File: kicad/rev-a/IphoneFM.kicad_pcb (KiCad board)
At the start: 2 copper layers, 46.5 x 71.4 mm, 106 parts, among them J1 USB 2.0 Type-C, J2 SMA jack, SW1 SPDT, SW2 SPST, SW3 6 × SPST, U1 MCU, U2 Synthesizer, U3 3.3 V 600 mA LDO, U4 FM receiver, U5 SPDT RF switch, U6 USB ESD array, U7 Digital step attenuator, Y2 20 MHz CMOS XO

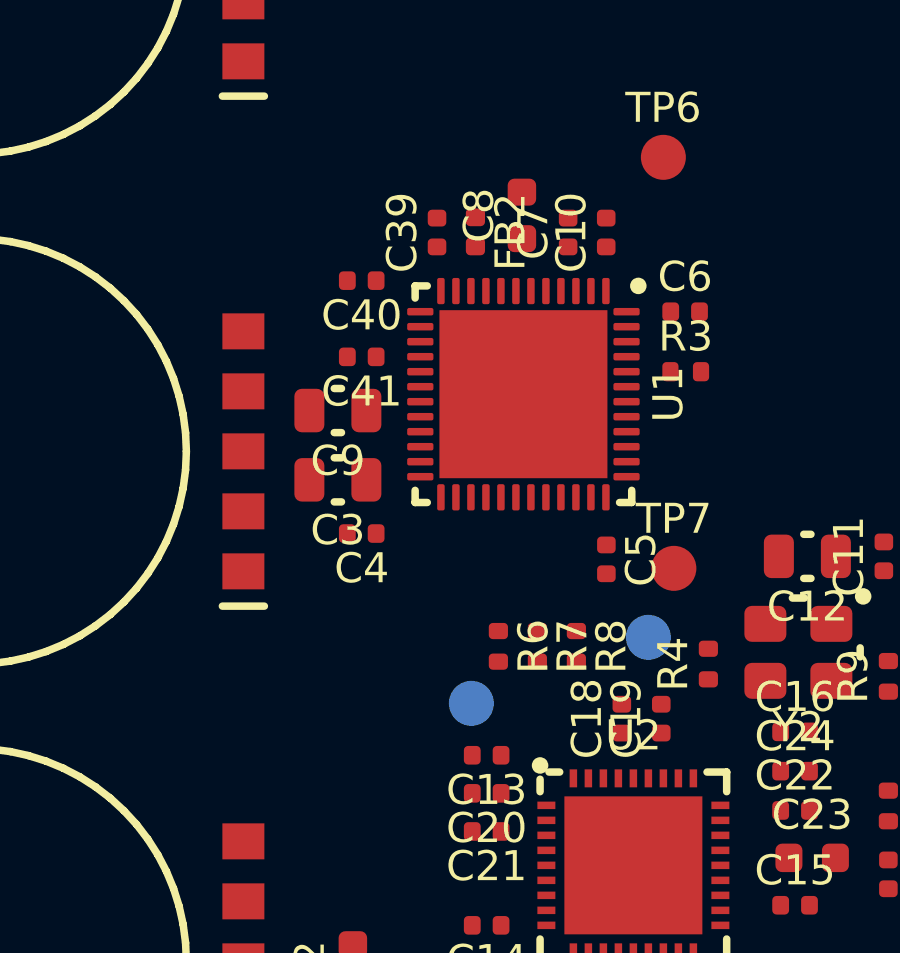
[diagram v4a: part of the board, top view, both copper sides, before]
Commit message: Phase 5 WIP: pcb_plan.py fan geometry, U1 escape plan (west and south, in progress), checker refinements; U1's west capacitors re-seated
Co-Authored-By: Claude Opus 5.5 <noreply@anthropic.com>
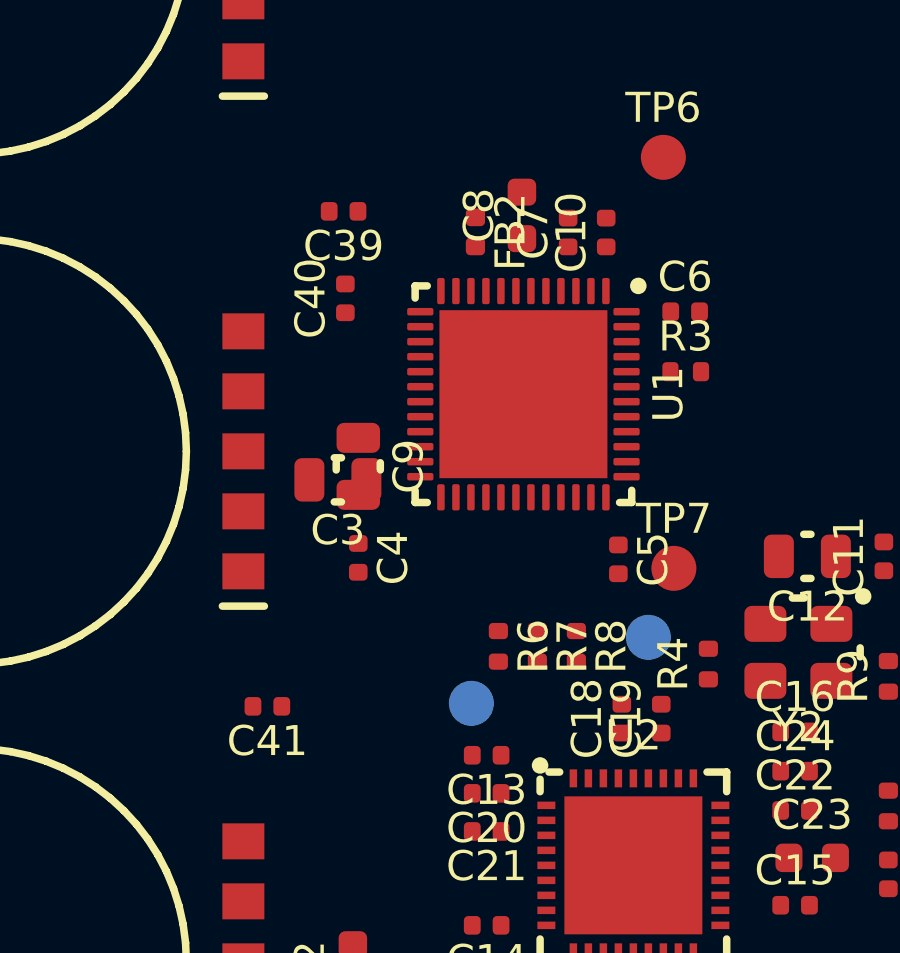
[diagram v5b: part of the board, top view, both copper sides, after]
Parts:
- moved C41 12.1 mm to (27.6, 103.5)
- moved C39 3.19 mm to (30.1, 87.0), turned to 180 degrees
- moved C9 1.98 mm to (30.6, 95.5), turned to -90 degrees
- moved C4 0.82 mm to (30.6, 98.5), turned to -90 degrees
- moved C40 0.80 mm to (30.2, 89.9), turned to 90 degrees
- moved C5 0.40 mm to (39.3, 98.6)
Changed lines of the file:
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@@
 	(footprint "IphoneFM:C_0402_1005Metric"
 		(layer "F.Cu")
-		(at 30.745 97.74 180)
+		(at 30.63 98.55 -90)
 		(descr "Capacitor SMD 0402 (1005 Metric), square (rectangular) end terminal, IPC-7351 nominal, (Body size source: IPC-SM-782 page 76, https://www.pcb-3d.com/wordpress/wp-content/uploads/ipc-sm-782a_amendment_1_and_2.pdf)")
 		(tags "capacitor")
 		(property "Reference" "C4"
-			(at 0 -1.16 540)
+			(at 0 -1.16 270)
 			(layer "F.SilkS")
 			(effects
@@
 		)
 		(property "Value" "100 nF X7R 16 V"
-			(at 0 1.16 540)
+			(at 0 1.16 270)
 			(layer "F.Fab")
 			(effects
@@
 		)
 		(property "Datasheet" "~"
-			(at 0 0 540)
+			(at 0 0 270)
 			(layer "F.Fab")
 			(hide yes)
@@
 		)
 		(property "Description" ""
-			(at 0 0 540)
+			(at 0 0 270)
 			(layer "F.Fab")
 			(hide yes)
@@
 		)
 		(property "KiLib_Generator" "SMD_2terminal_chip_molded"
-			(at 0 0 540)
+			(at 0 0 270)
 			(layer "F.SilkS")
 			(hide yes)
@@
 		)
 		(property "MPN" "CL05B104KO5NNNC"
-			(at 0 0 540)
+			(at 0 0 270)
 			(unlocked yes)
 			(layer "F.Fab")
@@
 		)
 		(property "LCSC" "C1525"
-			(at 0 0 540)
+			(at 0 0 270)
 			(unlocked yes)
 			(layer "F.Fab")
@@
 		)
 		(property "Manufacturer" "Samsung"
-			(at 0 0 540)
+			(at 0 0 270)
 			(unlocked yes)
 			(layer "F.Fab")
@@
 		)
 		(fp_text user "${REFERENCE}"
-			(at 0 0 540)
+			(at 0 0 630)
 			(layer "F.Fab")
 			(effects
@@
 		)
 		(pad "1" smd roundrect
-			(at -0.48 0 180)
+			(at -0.48 0 270)
 			(size 0.56 0.62)
 			(layers "F.Cu" "F.Mask" "F.Paste")
@@
 		)
 		(pad "2" smd roundrect
-			(at 0.48 0 180)
+			(at 0.48 0 270)
 			(size 0.56 0.62)
 			(layers "F.Cu" "F.Mask" "F.Paste")
@@
 	(footprint "IphoneFM:C_0402_1005Metric"
 		(layer "F.Cu")
-		(at 33.255 87.705 90)
+		(at 30.14 87 180)
 		(descr "Capacitor SMD 0402 (1005 Metric), square (rectangular) end terminal, IPC-7351 nominal, (Body size source: IPC-SM-782 page 76, https://www.pcb-3d.com/wordpress/wp-content/uploads/ipc-sm-782a_amendment_1_and_2.pdf)")
 		(tags "capacitor")
 		(property "Reference" "C39"
-			(at 0 -1.16 90)
+			(at 0 -1.16 180)
 			(layer "F.SilkS")
 			(effects
@@
 		)
 		(property "Value" "100 nF X7R 16 V"
-			(at 0 1.16 90)
+			(at 0 1.16 180)
 			(layer "F.Fab")
 			(effects
@@
 		)
 		(property "Datasheet" "~"
-			(at 0 0 90)
+			(at 0 0 180)
 			(layer "F.Fab")
 			(hide yes)
@@
 		)
 		(property "Description" ""
-			(at 0 0 90)
+			(at 0 0 180)
 			(layer "F.Fab")
 			(hide yes)
@@
 		)
 		(property "KiLib_Generator" "SMD_2terminal_chip_molded"
-			(at 0 0 90)
+			(at 0 0 180)
 			(layer "F.SilkS")
 			(hide yes)
@@
 		)
 		(property "MPN" "CL05B104KO5NNNC"
-			(at 0 0 90)
+			(at 0 0 180)
 			(unlocked yes)
 			(layer "F.Fab")
@@
 		)
 		(property "LCSC" "C1525"
-			(at 0 0 90)
+			(at 0 0 180)
 			(unlocked yes)
 			(layer "F.Fab")
@@
 		)
 		(property "Manufacturer" "Samsung"
-			(at 0 0 90)
+			(at 0 0 180)
 			(unlocked yes)
 			(layer "F.Fab")
@@
 		)
 		(fp_text user "${REFERENCE}"
-			(at 0 0 450)
+			(at 0 0 540)
 			(layer "F.Fab")
 			(effects
@@
 		)
 		(pad "1" smd roundrect
-			(at -0.48 0 90)
+			(at -0.48 0 180)
 			(size 0.56 0.62)
 			(layers "F.Cu" "F.Mask" "F.Paste")
@@
 		)
 		(pad "2" smd roundrect
-			(at 0.48 0 90)
+			(at 0.48 0 180)
 			(size 0.56 0.62)
 			(layers "F.Cu" "F.Mask" "F.Paste")
@@
 	(footprint "IphoneFM:C_0402_1005Metric"
 		(layer "F.Cu")
-		(at 38.9 98.6 -90)
+		(at 39.3 98.6 -90)
 		(descr "Capacitor SMD 0402 (1005 Metric), square (rectangular) end terminal, IPC-7351 nominal, (Body size source: IPC-SM-782 page 76, https://www.pcb-3d.com/wordpress/wp-content/uploads/ipc-sm-782a_amendment_1_and_2.pdf)")
 		(tags "capacitor")
@@
 	(footprint "IphoneFM:C_0805_2012Metric"
 		(layer "F.Cu")
-		(at 29.95 93.64 180)
+		(at 30.63 95.5 -90)
 		(descr "Capacitor SMD 0805 (2012 Metric), square (rectangular) end terminal, IPC-7351 nominal, (Body size source: IPC-SM-782 page 76, https://www.pcb-3d.com/wordpress/wp-content/uploads/ipc-sm-782a_amendment_1_and_2.pdf, https://docs.google.com/spreadsheets/d/1BsfQQcO9C6DZCsRaXUlFlo91Tg2WpOkGARC1WS5S8t0/edit?usp=sharing)")
 		(tags "capacitor")
 		(property "Reference" "C9"
-			(at 0 -1.68 540)
+			(at 0 -1.68 270)
 			(layer "F.SilkS")
 			(effects
@@
 		)
 		(property "Value" "4.7 µF X7R 16 V"
-			(at 0 1.68 540)
+			(at 0 1.68 270)
 			(layer "F.Fab")
 			(effects
@@
 		)
 		(property "Datasheet" "~"
-			(at 0 0 540)
+			(at 0 0 270)
 			(layer "F.Fab")
 			(hide yes)
@@
 		)
 		(property "Description" ""
-			(at 0 0 540)
+			(at 0 0 270)
 			(layer "F.Fab")
 			(hide yes)
@@
 		)
 		(property "KiLib_Generator" "SMD_2terminal_chip_molded"
-			(at 0 0 540)
+			(at 0 0 270)
 			(layer "F.SilkS")
 			(hide yes)
@@
 		)
 		(property "MPN" "GRM21BR71C475KE51L"
-			(at 0 0 540)
+			(at 0 0 270)
 			(unlocked yes)
 			(layer "F.Fab")
@@
 		)
 		(property "LCSC" "C408144"
-			(at 0 0 540)
+			(at 0 0 270)
 			(unlocked yes)
 			(layer "F.Fab")
@@
 		)
 		(property "Manufacturer" "Murata"
-			(at 0 0 540)
+			(at 0 0 270)
 			(unlocked yes)
 			(layer "F.Fab")
@@
 		(duplicate_pad_numbers_are_jumpers no)
 		(fp_line
-			(start -0.120599 -0.735)
-			(end 0.1206 -0.735)
+			(start -0.1206 0.735)
+			(end 0.120598 0.735)
 			(stroke
 				(width 0.25)
@@
 		)
 		(fp_line
-			(start -0.1206 0.735)
-			(end 0.120599 0.735)
+			(start -0.120598 -0.735)
+			(end 0.1206 -0.735)
 			(stroke
 				(width 0.25)
@@
 		)
 		(fp_text user "${REFERENCE}"
-			(at 0 0 540)
+			(at 0 0 630)
 			(layer "F.Fab")
 			(effects
@@
 		)
 		(pad "1" smd roundrect
-			(at -0.95 0 180)
+			(at -0.95 0 270)
 			(size 1 1.45)
 			(layers "F.Cu" "F.Mask" "F.Paste")
@@
 		)
 		(pad "2" smd roundrect
-			(at 0.95 0 180)
+			(at 0.95 0 270)
 			(size 1 1.45)
 			(layers "F.Cu" "F.Mask" "F.Paste")
@@
 	(footprint "IphoneFM:C_0402_1005Metric"
 		(layer "F.Cu")
-		(at 30.745 91.85 180)
+		(at 27.6 103.5 180)
 		(descr "Capacitor SMD 0402 (1005 Metric), square (rectangular) end terminal, IPC-7351 nominal, (Body size source: IPC-SM-782 page 76, https://www.pcb-3d.com/wordpress/wp-content/uploads/ipc-sm-782a_amendment_1_and_2.pdf)")
 		(tags "capacitor")
@@
 	(footprint "IphoneFM:C_0402_1005Metric"
 		(layer "F.Cu")
-		(at 30.745 89.31 180)
+		(at 30.2 89.9 90)
 		(descr "Capacitor SMD 0402 (1005 Metric), square (rectangular) end terminal, IPC-7351 nominal, (Body size source: IPC-SM-782 page 76, https://www.pcb-3d.com/wordpress/wp-content/uploads/ipc-sm-782a_amendment_1_and_2.pdf)")
 		(tags "capacitor")
 		(property "Reference" "C40"
-			(at 0 -1.16 540)
+			(at 0 -1.16 450)
 			(layer "F.SilkS")
 			(effects
@@
 		)
 		(property "Value" "100 nF X7R 16 V"
-			(at 0 1.16 540)
+			(at 0 1.16 450)
 			(layer "F.Fab")
 			(effects
@@
 		)
 		(property "Datasheet" "~"
-			(at 0 0 540)
+			(at 0 0 450)
 			(layer "F.Fab")
 			(hide yes)
@@
 		)
 		(property "Description" ""
-			(at 0 0 540)
+			(at 0 0 450)
 			(layer "F.Fab")
 			(hide yes)
@@
 		)
 		(property "KiLib_Generator" "SMD_2terminal_chip_molded"
-			(at 0 0 540)
+			(at 0 0 450)
 			(layer "F.SilkS")
 			(hide yes)
@@
 		)
 		(property "MPN" "CL05B104KO5NNNC"
-			(at 0 0 540)
+			(at 0 0 450)
 			(unlocked yes)
 			(layer "F.Fab")
@@
 		)
 		(property "LCSC" "C1525"
-			(at 0 0 540)
+			(at 0 0 450)
 			(unlocked yes)
 			(layer "F.Fab")
@@
 		)
 		(property "Manufacturer" "Samsung"
-			(at 0 0 540)
+			(at 0 0 450)
 			(unlocked yes)
 			(layer "F.Fab")
@@
 		(duplicate_pad_numbers_are_jumpers no)
 		(fp_rect
-			(start -0.909999 -0.46)
-			(end 0.909999 0.46)
+			(start -0.909998 -0.46)
+			(end 0.909998 0.46)
 			(stroke
 				(width 0.05)
@@
 		)
 		(fp_rect
-			(start -0.499999 -0.25)
-			(end 0.499999 0.25)
+			(start -0.499998 -0.25)
+			(end 0.499998 0.25)
 			(stroke
 				(width 0.1)
@@
 		)
 		(fp_text user "${REFERENCE}"
-			(at 0 0 540)
+			(at 0 0 810)
 			(layer "F.Fab")
 			(effects
@@
 		)
 		(pad "1" smd roundrect
-			(at -0.48 0 180)
+			(at -0.48 0 90)
 			(size 0.56 0.62)
 			(layers "F.Cu" "F.Mask" "F.Paste")
@@
 		)
 		(pad "2" smd roundrect
-			(at 0.48 0 180)
+			(at 0.48 0 90)
 			(size 0.56 0.62)
 			(layers "F.Cu" "F.Mask" "F.Paste")

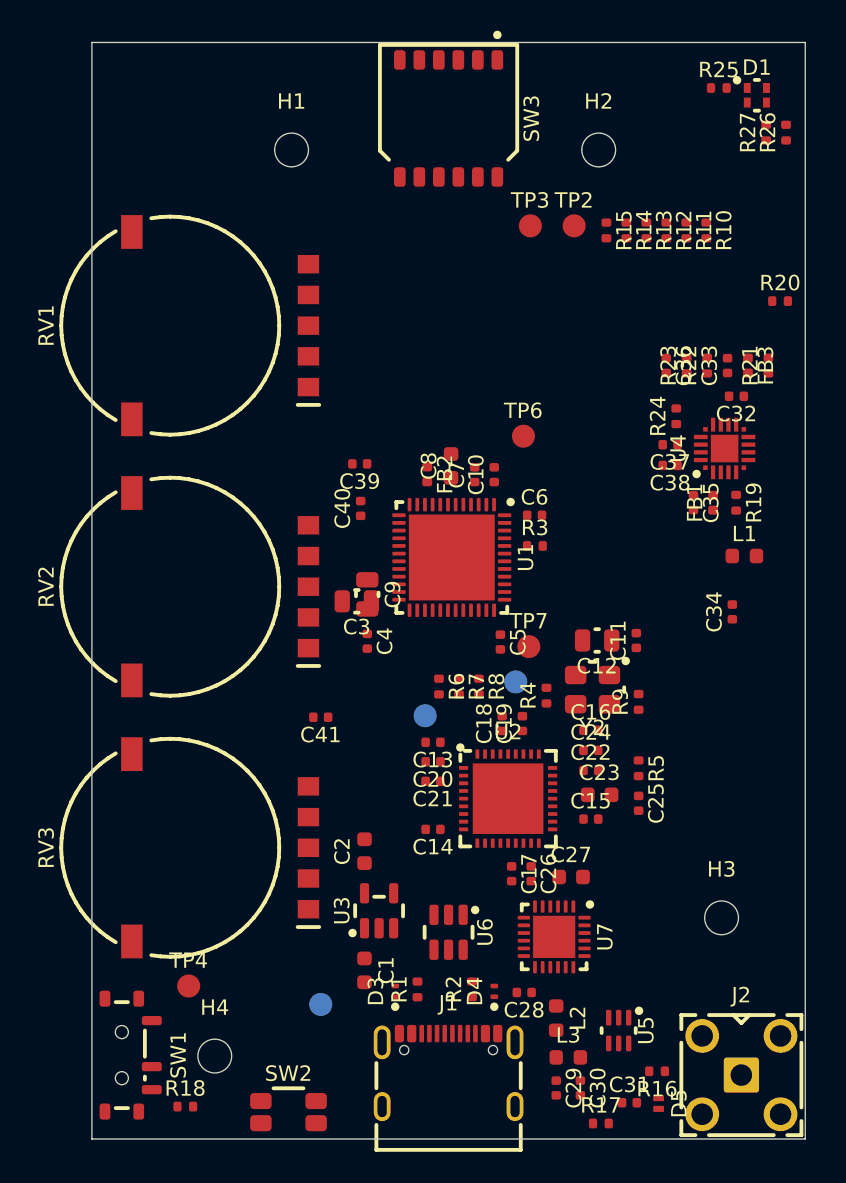
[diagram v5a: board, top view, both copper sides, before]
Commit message: Phase 5 prep: U1 escape at its new position, U2 plan (pcb_route_u2.py), U6 channels swapped
U1 sits at (36.135, 90.595) with its escape planned on all four sides; the U2 plan covers U2's
pins and parts (FSK with the clock hop, MICROWIRE, the PLL capacitor column, CE, REF20, 3V3
feeds), the USB pair under U2 up north of U6 (0.7 mm lower) and the two bottom 3V3 links in the
RF zone the user allowed (RF_BOTTOM_ALLOW). Checker: local pins now count branches; 0 findings
over the U1, U4, RF and U2 plans. U6's ESD channels swapped in the schematic and netlist.

Co-Authored-By: Claude Opus 5.5 <noreply@anthropic.com>
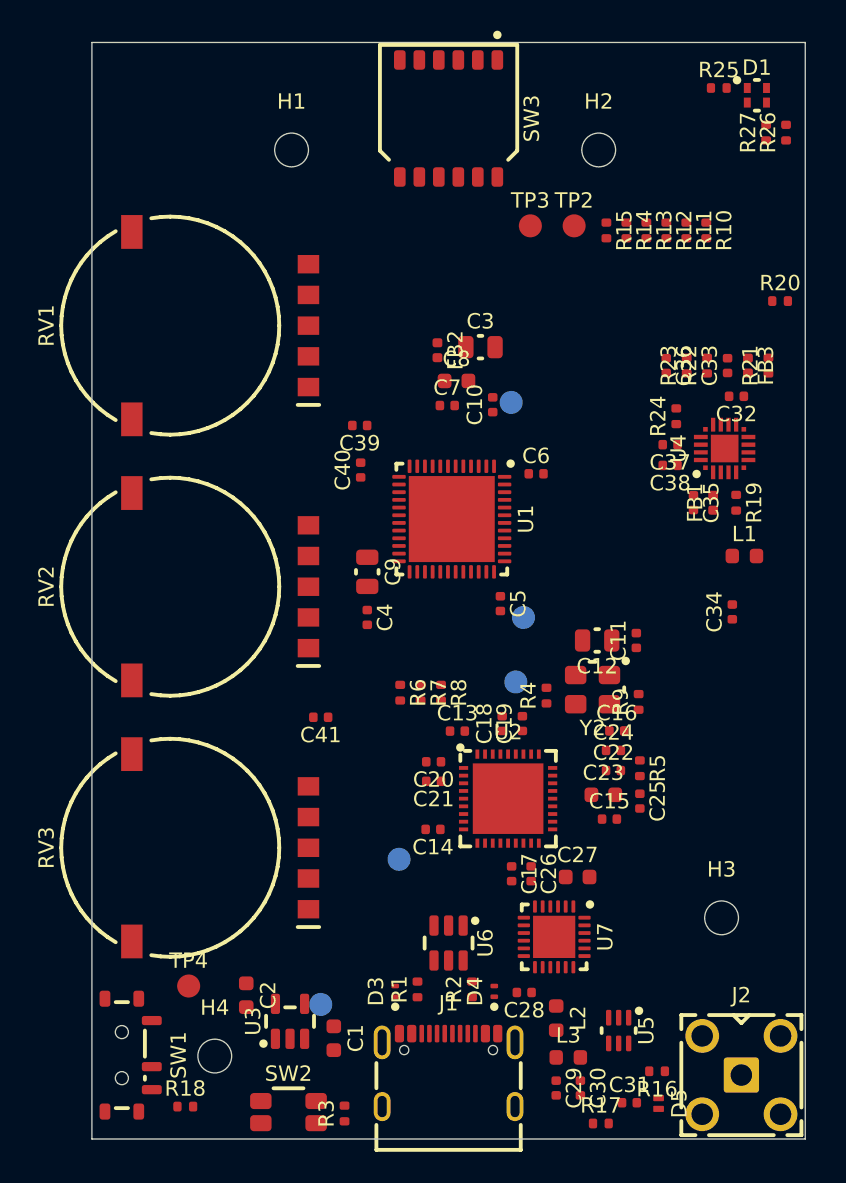
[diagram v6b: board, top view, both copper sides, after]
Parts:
- TP6, TP7: moved to B.Cu
- moved R3 39.0 mm to (29.1, 129.3), turned to 90 degrees
- moved C3 18.4 mm to (38.0, 79.4), turned to 0 degrees
- moved C2 12.1 mm to (22.8, 121.6), turned to -90 degrees
- moved TP5 9.50 mm to (32.7, 112.8)
- moved U3 9.25 mm to (25.6, 123.3)
- moved FB2 8.11 mm to (35.2, 79.6)
- moved C8 5.55 mm to (36.4, 81.6), turned to 0 degrees
- moved C1 4.85 mm to (28.4, 124.4)
- moved C7 4.85 mm to (35.8, 83.2), turned to 0 degrees
- moved C10 4.56 mm to (38.8, 83.2)
- moved C6 2.70 mm to (41.6, 87.6)
- moved R6 2.56 mm to (32.8, 101.9)
- moved R7 2.53 mm to (34.1, 101.9)
- moved C39 2.50 mm to (30.1, 84.5)
- moved C40 2.50 mm to (30.2, 87.4)
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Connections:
- U6 pad 1: /USB_DM -> /USB_DP
- U6 pad 3: /USB_DP -> /USB_DM
- U6 pad 4: /USB_DP -> /USB_DM
- U6 pad 6: /USB_DM -> /USB_DP
